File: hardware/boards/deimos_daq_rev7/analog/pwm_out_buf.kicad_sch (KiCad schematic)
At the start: 3 parts

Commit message: wip to update layout for frontend
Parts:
- renumbered D55001 to D19001, R55001 to R19001, R55002 to R19002
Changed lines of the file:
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@@
 		(on_board yes)
 		(dnp no)
-		(property "Reference" "#PWR277"
+		(property "Reference" "#PWR19005"
 			(at 143.764 106.426 0)
 			(effects
@@
 		)
 		(instances
-			(project "analog_i"
-				(path "/5a60c4b1-b6cb-416e-8883-8291fa089b87/c2baf18d-2b19-4edb-98b3-535275ee271f/2a5a8a5b-3176-4558-a595-780d8191c46b"
-					(reference "#PWR282")
-					(unit 1)
-				)
-				(path "/5a60c4b1-b6cb-416e-8883-8291fa089b87/c2baf18d-2b19-4edb-98b3-535275ee271f/3d57a2e8-76a3-4b72-b88d-c02ba9a3137f"
-					(reference "#PWR277")
-					(unit 1)
-				)
-				(path "/5a60c4b1-b6cb-416e-8883-8291fa089b87/c2baf18d-2b19-4edb-98b3-535275ee271f/489c5c16-982c-4958-8e55-03934daf9e33"
-					(reference "#PWR312")
-					(unit 1)
-				)
-				(path "/5a60c4b1-b6cb-416e-8883-8291fa089b87/c2baf18d-2b19-4edb-98b3-535275ee271f/ae776014-17b3-402b-a4e6-eaff991cef75"
-					(reference "#PWR307")
-					(unit 1)
-				)
-				(path "/5a60c4b1-b6cb-416e-8883-8291fa089b87/c2baf18d-2b19-4edb-98b3-535275ee271f/d8ba479a-a7d9-47f0-902a-0be012b7ebf9"
-					(reference "#PWR302")
-					(unit 1)
-				)
-				(path "/5a60c4b1-b6cb-416e-8883-8291fa089b87/c2baf18d-2b19-4edb-98b3-535275ee271f/e5d59c3a-5602-4acb-ba66-19187ee13f4f"
-					(reference "#PWR367")
-					(unit 1)
-				)
-				(path "/5a60c4b1-b6cb-416e-8883-8291fa089b87/c2baf18d-2b19-4edb-98b3-535275ee271f/fbe215fd-185e-4781-8db8-c963f195ff3e"
-					(reference "#PWR287")
-					(unit 1)
-				)
-			)
 			(project "analog_frontend_panel"
 				(path "/c241d083-1323-4b4a-a540-956d0afb7b72/2a5a8a5b-3176-4558-a595-780d8191c46b"
@@
 				(path "/c241d083-1323-4b4a-a540-956d0afb7b72/ae776014-17b3-402b-a4e6-eaff991cef75"
 					(reference "#PWR47007")
+					(unit 1)
+				)
+				(path "/c241d083-1323-4b4a-a540-956d0afb7b72/d157c6a6-e46c-46fa-8790-e34cb70ef5c4"
+					(reference "#PWR50002")
 					(unit 1)
 				)
@@
 		(on_board yes)
 		(dnp no)
-		(property "Reference" "#PWR274"
+		(property "Reference" "#PWR19001"
 			(at 128.016 103.886 0)
 			(effects
@@
 		)
 		(instances
-			(project "analog_i"
-				(path "/5a60c4b1-b6cb-416e-8883-8291fa089b87/c2baf18d-2b19-4edb-98b3-535275ee271f/2a5a8a5b-3176-4558-a595-780d8191c46b"
-					(reference "#PWR279")
-					(unit 1)
-				)
-				(path "/5a60c4b1-b6cb-416e-8883-8291fa089b87/c2baf18d-2b19-4edb-98b3-535275ee271f/3d57a2e8-76a3-4b72-b88d-c02ba9a3137f"
-					(reference "#PWR274")
-					(unit 1)
-				)
-				(path "/5a60c4b1-b6cb-416e-8883-8291fa089b87/c2baf18d-2b19-4edb-98b3-535275ee271f/489c5c16-982c-4958-8e55-03934daf9e33"
-					(reference "#PWR308")
-					(unit 1)
-				)
-				(path "/5a60c4b1-b6cb-416e-8883-8291fa089b87/c2baf18d-2b19-4edb-98b3-535275ee271f/ae776014-17b3-402b-a4e6-eaff991cef75"
-					(reference "#PWR303")
-					(unit 1)
-				)
-				(path "/5a60c4b1-b6cb-416e-8883-8291fa089b87/c2baf18d-2b19-4edb-98b3-535275ee271f/d8ba479a-a7d9-47f0-902a-0be012b7ebf9"
-					(reference "#PWR298")
-					(unit 1)
-				)
-				(path "/5a60c4b1-b6cb-416e-8883-8291fa089b87/c2baf18d-2b19-4edb-98b3-535275ee271f/e5d59c3a-5602-4acb-ba66-19187ee13f4f"
-					(reference "#PWR366")
-					(unit 1)
-				)
-				(path "/5a60c4b1-b6cb-416e-8883-8291fa089b87/c2baf18d-2b19-4edb-98b3-535275ee271f/fbe215fd-185e-4781-8db8-c963f195ff3e"
-					(reference "#PWR284")
-					(unit 1)
-				)
-			)
 			(project "analog_frontend_panel"
 				(path "/c241d083-1323-4b4a-a540-956d0afb7b72/2a5a8a5b-3176-4558-a595-780d8191c46b"
@@
 				(path "/c241d083-1323-4b4a-a540-956d0afb7b72/ae776014-17b3-402b-a4e6-eaff991cef75"
 					(reference "#PWR47003")
+					(unit 1)
+				)
+				(path "/c241d083-1323-4b4a-a540-956d0afb7b72/d157c6a6-e46c-46fa-8790-e34cb70ef5c4"
+					(reference "#PWR50001")
 					(unit 1)
 				)
@@
 		(on_board yes)
 		(dnp no)
-		(property "Reference" "R55002"
+		(property "Reference" "R19002"
 			(at 154.686 96.774 90)
 			(effects
@@
 		)
 		(instances
-			(project "analog_i"
-				(path "/5a60c4b1-b6cb-416e-8883-8291fa089b87/c2baf18d-2b19-4edb-98b3-535275ee271f/2a5a8a5b-3176-4558-a595-780d8191c46b"
-					(reference "R56002")
-					(unit 1)
-				)
-				(path "/5a60c4b1-b6cb-416e-8883-8291fa089b87/c2baf18d-2b19-4edb-98b3-535275ee271f/3d57a2e8-76a3-4b72-b88d-c02ba9a3137f"
-					(reference "R55002")
-					(unit 1)
-				)
-				(path "/5a60c4b1-b6cb-416e-8883-8291fa089b87/c2baf18d-2b19-4edb-98b3-535275ee271f/489c5c16-982c-4958-8e55-03934daf9e33"
-					(reference "R60002")
-					(unit 1)
-				)
-				(path "/5a60c4b1-b6cb-416e-8883-8291fa089b87/c2baf18d-2b19-4edb-98b3-535275ee271f/ae776014-17b3-402b-a4e6-eaff991cef75"
-					(reference "R59002")
-					(unit 1)
-				)
-				(path "/5a60c4b1-b6cb-416e-8883-8291fa089b87/c2baf18d-2b19-4edb-98b3-535275ee271f/d8ba479a-a7d9-47f0-902a-0be012b7ebf9"
-					(reference "R58002")
-					(unit 1)
-				)
-				(path "/5a60c4b1-b6cb-416e-8883-8291fa089b87/c2baf18d-2b19-4edb-98b3-535275ee271f/e5d59c3a-5602-4acb-ba66-19187ee13f4f"
-					(reference "R64002")
-					(unit 1)
-				)
-				(path "/5a60c4b1-b6cb-416e-8883-8291fa089b87/c2baf18d-2b19-4edb-98b3-535275ee271f/fbe215fd-185e-4781-8db8-c963f195ff3e"
-					(reference "R57002")
-					(unit 1)
-				)
-			)
 			(project "analog_frontend_panel"
 				(path "/c241d083-1323-4b4a-a540-956d0afb7b72/2a5a8a5b-3176-4558-a595-780d8191c46b"
@@
 				(path "/c241d083-1323-4b4a-a540-956d0afb7b72/ae776014-17b3-402b-a4e6-eaff991cef75"
 					(reference "R47004")
+					(unit 1)
+				)
+				(path "/c241d083-1323-4b4a-a540-956d0afb7b72/d157c6a6-e46c-46fa-8790-e34cb70ef5c4"
+					(reference "R50002")
 					(unit 1)
 				)
@@
 		(on_board yes)
 		(dnp no)
-		(property "Reference" "R55001"
+		(property "Reference" "R19001"
 			(at 129.286 94.996 0)
 			(effects
@@
 		)
 		(instances
-			(project "analog_i"
-				(path "/5a60c4b1-b6cb-416e-8883-8291fa089b87/c2baf18d-2b19-4edb-98b3-535275ee271f/2a5a8a5b-3176-4558-a595-780d8191c46b"
-					(reference "R56001")
-					(unit 1)
-				)
-				(path "/5a60c4b1-b6cb-416e-8883-8291fa089b87/c2baf18d-2b19-4edb-98b3-535275ee271f/3d57a2e8-76a3-4b72-b88d-c02ba9a3137f"
-					(reference "R55001")
-					(unit 1)
-				)
-				(path "/5a60c4b1-b6cb-416e-8883-8291fa089b87/c2baf18d-2b19-4edb-98b3-535275ee271f/489c5c16-982c-4958-8e55-03934daf9e33"
-					(reference "R60001")
-					(unit 1)
-				)
-				(path "/5a60c4b1-b6cb-416e-8883-8291fa089b87/c2baf18d-2b19-4edb-98b3-535275ee271f/ae776014-17b3-402b-a4e6-eaff991cef75"
-					(reference "R59001")
-					(unit 1)
-				)
-				(path "/5a60c4b1-b6cb-416e-8883-8291fa089b87/c2baf18d-2b19-4edb-98b3-535275ee271f/d8ba479a-a7d9-47f0-902a-0be012b7ebf9"
-					(reference "R58001")
-					(unit 1)
-				)
-				(path "/5a60c4b1-b6cb-416e-8883-8291fa089b87/c2baf18d-2b19-4edb-98b3-535275ee271f/e5d59c3a-5602-4acb-ba66-19187ee13f4f"
-					(reference "R64001")
-					(unit 1)
-				)
-				(path "/5a60c4b1-b6cb-416e-8883-8291fa089b87/c2baf18d-2b19-4edb-98b3-535275ee271f/fbe215fd-185e-4781-8db8-c963f195ff3e"
-					(reference "R57001")
-					(unit 1)
-				)
-			)
 			(project "analog_frontend_panel"
 				(path "/c241d083-1323-4b4a-a540-956d0afb7b72/2a5a8a5b-3176-4558-a595-780d8191c46b"
@@
 				(path "/c241d083-1323-4b4a-a540-956d0afb7b72/ae776014-17b3-402b-a4e6-eaff991cef75"
 					(reference "R47003")
+					(unit 1)
+				)
+				(path "/c241d083-1323-4b4a-a540-956d0afb7b72/d157c6a6-e46c-46fa-8790-e34cb70ef5c4"
+					(reference "R50001")
 					(unit 1)
 				)
@@
 		(on_board yes)
 		(dnp no)
-		(property "Reference" "D55001"
+		(property "Reference" "D19001"
 			(at 140.97 96.266 0)
 			(effects
@@
 		)
 		(instances
-			(project "analog_i"
-				(path "/5a60c4b1-b6cb-416e-8883-8291fa089b87/c2baf18d-2b19-4edb-98b3-535275ee271f/2a5a8a5b-3176-4558-a595-780d8191c46b"
-					(reference "D56001")
-					(unit 1)
-				)
-				(path "/5a60c4b1-b6cb-416e-8883-8291fa089b87/c2baf18d-2b19-4edb-98b3-535275ee271f/3d57a2e8-76a3-4b72-b88d-c02ba9a3137f"
-					(reference "D55001")
-					(unit 1)
-				)
-				(path "/5a60c4b1-b6cb-416e-8883-8291fa089b87/c2baf18d-2b19-4edb-98b3-535275ee271f/489c5c16-982c-4958-8e55-03934daf9e33"
-					(reference "D60001")
-					(unit 1)
-				)
-				(path "/5a60c4b1-b6cb-416e-8883-8291fa089b87/c2baf18d-2b19-4edb-98b3-535275ee271f/ae776014-17b3-402b-a4e6-eaff991cef75"
-					(reference "D59001")
-					(unit 1)
-				)
-				(path "/5a60c4b1-b6cb-416e-8883-8291fa089b87/c2baf18d-2b19-4edb-98b3-535275ee271f/d8ba479a-a7d9-47f0-902a-0be012b7ebf9"
-					(reference "D58001")
-					(unit 1)
-				)
-				(path "/5a60c4b1-b6cb-416e-8883-8291fa089b87/c2baf18d-2b19-4edb-98b3-535275ee271f/e5d59c3a-5602-4acb-ba66-19187ee13f4f"
-					(reference "D64001")
-					(unit 1)
-				)
-				(path "/5a60c4b1-b6cb-416e-8883-8291fa089b87/c2baf18d-2b19-4edb-98b3-535275ee271f/fbe215fd-185e-4781-8db8-c963f195ff3e"
-					(reference "D57001")
-					(unit 1)
-				)
-			)
 			(project "analog_frontend_panel"
 				(path "/c241d083-1323-4b4a-a540-956d0afb7b72/2a5a8a5b-3176-4558-a595-780d8191c46b"
@@
 					(unit 1)
 				)
+				(path "/c241d083-1323-4b4a-a540-956d0afb7b72/d157c6a6-e46c-46fa-8790-e34cb70ef5c4"
+					(reference "D50001")
+					(unit 1)
+				)

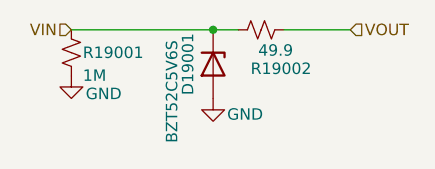
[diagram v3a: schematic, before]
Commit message: wip to update silkscreen
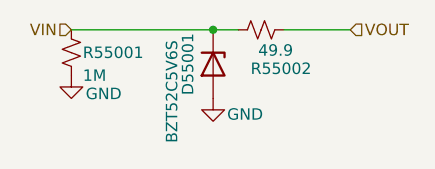
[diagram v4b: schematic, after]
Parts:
- renumbered D19001 to D55001, R19001 to R55001, R19002 to R55002
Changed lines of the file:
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@@
 		(on_board yes)
 		(dnp no)
-		(property "Reference" "#PWR19005"
+		(property "Reference" "#PWR277"
 			(at 143.764 106.426 0)
 			(effects
@@
 		)
 		(instances
+			(project "analog_i"
+				(path "/5a60c4b1-b6cb-416e-8883-8291fa089b87/c2baf18d-2b19-4edb-98b3-535275ee271f/2a5a8a5b-3176-4558-a595-780d8191c46b"
+					(reference "#PWR282")
+					(unit 1)
+				)
+				(path "/5a60c4b1-b6cb-416e-8883-8291fa089b87/c2baf18d-2b19-4edb-98b3-535275ee271f/3d57a2e8-76a3-4b72-b88d-c02ba9a3137f"
+					(reference "#PWR277")
+					(unit 1)
+				)
+				(path "/5a60c4b1-b6cb-416e-8883-8291fa089b87/c2baf18d-2b19-4edb-98b3-535275ee271f/489c5c16-982c-4958-8e55-03934daf9e33"
+					(reference "#PWR312")
+					(unit 1)
+				)
+				(path "/5a60c4b1-b6cb-416e-8883-8291fa089b87/c2baf18d-2b19-4edb-98b3-535275ee271f/ae776014-17b3-402b-a4e6-eaff991cef75"
+					(reference "#PWR307")
+					(unit 1)
+				)
+				(path "/5a60c4b1-b6cb-416e-8883-8291fa089b87/c2baf18d-2b19-4edb-98b3-535275ee271f/d157c6a6-e46c-46fa-8790-e34cb70ef5c4"
+					(reference "#PWR317")
+					(unit 1)
+				)
+				(path "/5a60c4b1-b6cb-416e-8883-8291fa089b87/c2baf18d-2b19-4edb-98b3-535275ee271f/d8ba479a-a7d9-47f0-902a-0be012b7ebf9"
+					(reference "#PWR302")
+					(unit 1)
+				)
+				(path "/5a60c4b1-b6cb-416e-8883-8291fa089b87/c2baf18d-2b19-4edb-98b3-535275ee271f/e5d59c3a-5602-4acb-ba66-19187ee13f4f"
+					(reference "#PWR367")
+					(unit 1)
+				)
+				(path "/5a60c4b1-b6cb-416e-8883-8291fa089b87/c2baf18d-2b19-4edb-98b3-535275ee271f/fbe215fd-185e-4781-8db8-c963f195ff3e"
+					(reference "#PWR287")
+					(unit 1)
+				)
+			)
 			(project "analog_frontend_panel"
 				(path "/c241d083-1323-4b4a-a540-956d0afb7b72/2a5a8a5b-3176-4558-a595-780d8191c46b"
@@
 		(on_board yes)
 		(dnp no)
-		(property "Reference" "#PWR19001"
+		(property "Reference" "#PWR274"
 			(at 128.016 103.886 0)
 			(effects
@@
 		)
 		(instances
+			(project "analog_i"
+				(path "/5a60c4b1-b6cb-416e-8883-8291fa089b87/c2baf18d-2b19-4edb-98b3-535275ee271f/2a5a8a5b-3176-4558-a595-780d8191c46b"
+					(reference "#PWR279")
+					(unit 1)
+				)
+				(path "/5a60c4b1-b6cb-416e-8883-8291fa089b87/c2baf18d-2b19-4edb-98b3-535275ee271f/3d57a2e8-76a3-4b72-b88d-c02ba9a3137f"
+					(reference "#PWR274")
+					(unit 1)
+				)
+				(path "/5a60c4b1-b6cb-416e-8883-8291fa089b87/c2baf18d-2b19-4edb-98b3-535275ee271f/489c5c16-982c-4958-8e55-03934daf9e33"
+					(reference "#PWR308")
+					(unit 1)
+				)
+				(path "/5a60c4b1-b6cb-416e-8883-8291fa089b87/c2baf18d-2b19-4edb-98b3-535275ee271f/ae776014-17b3-402b-a4e6-eaff991cef75"
+					(reference "#PWR303")
+					(unit 1)
+				)
+				(path "/5a60c4b1-b6cb-416e-8883-8291fa089b87/c2baf18d-2b19-4edb-98b3-535275ee271f/d157c6a6-e46c-46fa-8790-e34cb70ef5c4"
+					(reference "#PWR313")
+					(unit 1)
+				)
+				(path "/5a60c4b1-b6cb-416e-8883-8291fa089b87/c2baf18d-2b19-4edb-98b3-535275ee271f/d8ba479a-a7d9-47f0-902a-0be012b7ebf9"
+					(reference "#PWR298")
+					(unit 1)
+				)
+				(path "/5a60c4b1-b6cb-416e-8883-8291fa089b87/c2baf18d-2b19-4edb-98b3-535275ee271f/e5d59c3a-5602-4acb-ba66-19187ee13f4f"
+					(reference "#PWR366")
+					(unit 1)
+				)
+				(path "/5a60c4b1-b6cb-416e-8883-8291fa089b87/c2baf18d-2b19-4edb-98b3-535275ee271f/fbe215fd-185e-4781-8db8-c963f195ff3e"
+					(reference "#PWR284")
+					(unit 1)
+				)
+			)
 			(project "analog_frontend_panel"
 				(path "/c241d083-1323-4b4a-a540-956d0afb7b72/2a5a8a5b-3176-4558-a595-780d8191c46b"
@@
 		(on_board yes)
 		(dnp no)
-		(property "Reference" "R19002"
+		(property "Reference" "R55002"
 			(at 154.686 96.774 90)
 			(effects
@@
 		)
 		(instances
+			(project "analog_i"
+				(path "/5a60c4b1-b6cb-416e-8883-8291fa089b87/c2baf18d-2b19-4edb-98b3-535275ee271f/2a5a8a5b-3176-4558-a595-780d8191c46b"
+					(reference "R56002")
+					(unit 1)
+				)
+				(path "/5a60c4b1-b6cb-416e-8883-8291fa089b87/c2baf18d-2b19-4edb-98b3-535275ee271f/3d57a2e8-76a3-4b72-b88d-c02ba9a3137f"
+					(reference "R55002")
+					(unit 1)
+				)
+				(path "/5a60c4b1-b6cb-416e-8883-8291fa089b87/c2baf18d-2b19-4edb-98b3-535275ee271f/489c5c16-982c-4958-8e55-03934daf9e33"
+					(reference "R60002")
+					(unit 1)
+				)
+				(path "/5a60c4b1-b6cb-416e-8883-8291fa089b87/c2baf18d-2b19-4edb-98b3-535275ee271f/ae776014-17b3-402b-a4e6-eaff991cef75"
+					(reference "R59002")
+					(unit 1)
+				)
+				(path "/5a60c4b1-b6cb-416e-8883-8291fa089b87/c2baf18d-2b19-4edb-98b3-535275ee271f/d157c6a6-e46c-46fa-8790-e34cb70ef5c4"
+					(reference "R61002")
+					(unit 1)
+				)
+				(path "/5a60c4b1-b6cb-416e-8883-8291fa089b87/c2baf18d-2b19-4edb-98b3-535275ee271f/d8ba479a-a7d9-47f0-902a-0be012b7ebf9"
+					(reference "R58002")
+					(unit 1)
+				)
+				(path "/5a60c4b1-b6cb-416e-8883-8291fa089b87/c2baf18d-2b19-4edb-98b3-535275ee271f/e5d59c3a-5602-4acb-ba66-19187ee13f4f"
+					(reference "R64002")
+					(unit 1)
+				)
+				(path "/5a60c4b1-b6cb-416e-8883-8291fa089b87/c2baf18d-2b19-4edb-98b3-535275ee271f/fbe215fd-185e-4781-8db8-c963f195ff3e"
+					(reference "R57002")
+					(unit 1)
+				)
+			)
 			(project "analog_frontend_panel"
 				(path "/c241d083-1323-4b4a-a540-956d0afb7b72/2a5a8a5b-3176-4558-a595-780d8191c46b"
@@
 		(on_board yes)
 		(dnp no)
-		(property "Reference" "R19001"
+		(property "Reference" "R55001"
 			(at 129.286 94.996 0)
 			(effects
@@
 		)
 		(instances
+			(project "analog_i"
+				(path "/5a60c4b1-b6cb-416e-8883-8291fa089b87/c2baf18d-2b19-4edb-98b3-535275ee271f/2a5a8a5b-3176-4558-a595-780d8191c46b"
+					(reference "R56001")
+					(unit 1)
+				)
+				(path "/5a60c4b1-b6cb-416e-8883-8291fa089b87/c2baf18d-2b19-4edb-98b3-535275ee271f/3d57a2e8-76a3-4b72-b88d-c02ba9a3137f"
+					(reference "R55001")
+					(unit 1)
+				)
+				(path "/5a60c4b1-b6cb-416e-8883-8291fa089b87/c2baf18d-2b19-4edb-98b3-535275ee271f/489c5c16-982c-4958-8e55-03934daf9e33"
+					(reference "R60001")
+					(unit 1)
+				)
+				(path "/5a60c4b1-b6cb-416e-8883-8291fa089b87/c2baf18d-2b19-4edb-98b3-535275ee271f/ae776014-17b3-402b-a4e6-eaff991cef75"
+					(reference "R59001")
+					(unit 1)
+				)
+				(path "/5a60c4b1-b6cb-416e-8883-8291fa089b87/c2baf18d-2b19-4edb-98b3-535275ee271f/d157c6a6-e46c-46fa-8790-e34cb70ef5c4"
+					(reference "R61001")
+					(unit 1)
+				)
+				(path "/5a60c4b1-b6cb-416e-8883-8291fa089b87/c2baf18d-2b19-4edb-98b3-535275ee271f/d8ba479a-a7d9-47f0-902a-0be012b7ebf9"
+					(reference "R58001")
+					(unit 1)
+				)
+				(path "/5a60c4b1-b6cb-416e-8883-8291fa089b87/c2baf18d-2b19-4edb-98b3-535275ee271f/e5d59c3a-5602-4acb-ba66-19187ee13f4f"
+					(reference "R64001")
+					(unit 1)
+				)
+				(path "/5a60c4b1-b6cb-416e-8883-8291fa089b87/c2baf18d-2b19-4edb-98b3-535275ee271f/fbe215fd-185e-4781-8db8-c963f195ff3e"
+					(reference "R57001")
+					(unit 1)
+				)
+			)
 			(project "analog_frontend_panel"
 				(path "/c241d083-1323-4b4a-a540-956d0afb7b72/2a5a8a5b-3176-4558-a595-780d8191c46b"
@@
 		(on_board yes)
 		(dnp no)
-		(property "Reference" "D19001"
+		(property "Reference" "D55001"
 			(at 140.97 96.266 0)
 			(effects
@@
 		)
 		(instances
+			(project "analog_i"
+				(path "/5a60c4b1-b6cb-416e-8883-8291fa089b87/c2baf18d-2b19-4edb-98b3-535275ee271f/2a5a8a5b-3176-4558-a595-780d8191c46b"
+					(reference "D56001")
+					(unit 1)
+				)
+				(path "/5a60c4b1-b6cb-416e-8883-8291fa089b87/c2baf18d-2b19-4edb-98b3-535275ee271f/3d57a2e8-76a3-4b72-b88d-c02ba9a3137f"
+					(reference "D55001")
+					(unit 1)
+				)
+				(path "/5a60c4b1-b6cb-416e-8883-8291fa089b87/c2baf18d-2b19-4edb-98b3-535275ee271f/489c5c16-982c-4958-8e55-03934daf9e33"
+					(reference "D60001")
+					(unit 1)
+				)
+				(path "/5a60c4b1-b6cb-416e-8883-8291fa089b87/c2baf18d-2b19-4edb-98b3-535275ee271f/ae776014-17b3-402b-a4e6-eaff991cef75"
+					(reference "D59001")
+					(unit 1)
+				)
+				(path "/5a60c4b1-b6cb-416e-8883-8291fa089b87/c2baf18d-2b19-4edb-98b3-535275ee271f/d157c6a6-e46c-46fa-8790-e34cb70ef5c4"
+					(reference "D61001")
+					(unit 1)
+				)
+				(path "/5a60c4b1-b6cb-416e-8883-8291fa089b87/c2baf18d-2b19-4edb-98b3-535275ee271f/d8ba479a-a7d9-47f0-902a-0be012b7ebf9"
+					(reference "D58001")
+					(unit 1)
+				)
+				(path "/5a60c4b1-b6cb-416e-8883-8291fa089b87/c2baf18d-2b19-4edb-98b3-535275ee271f/e5d59c3a-5602-4acb-ba66-19187ee13f4f"
+					(reference "D64001")
+					(unit 1)
+				)
+				(path "/5a60c4b1-b6cb-416e-8883-8291fa089b87/c2baf18d-2b19-4edb-98b3-535275ee271f/fbe215fd-185e-4781-8db8-c963f195ff3e"
+					(reference "D57001")
+					(unit 1)
+				)
+			)
 			(project "analog_frontend_panel"
 				(path "/c241d083-1323-4b4a-a540-956d0afb7b72/2a5a8a5b-3176-4558-a595-780d8191c46b"

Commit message: first pass adding dsub breakout schematic, routing, and labels
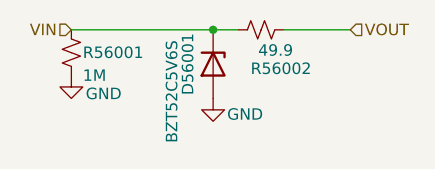
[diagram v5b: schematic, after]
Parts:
- renumbered D55001 to D56001, R55001 to R56001, R55002 to R56002
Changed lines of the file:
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@@
 		(on_board yes)
 		(dnp no)
-		(property "Reference" "#PWR277"
+		(property "Reference" "#PWR282"
 			(at 143.764 106.426 0)
 			(effects
@@
 		(on_board yes)
 		(dnp no)
-		(property "Reference" "#PWR274"
+		(property "Reference" "#PWR279"
 			(at 128.016 103.886 0)
 			(effects
@@
 		(on_board yes)
 		(dnp no)
-		(property "Reference" "R55002"
+		(property "Reference" "R56002"
 			(at 154.686 96.774 90)
 			(effects
@@
 		(on_board yes)
 		(dnp no)
-		(property "Reference" "R55001"
+		(property "Reference" "R56001"
 			(at 129.286 94.996 0)
 			(effects
@@
 		(on_board yes)
 		(dnp no)
-		(property "Reference" "D55001"
+		(property "Reference" "D56001"
 			(at 140.97 96.266 0)
 			(effects
